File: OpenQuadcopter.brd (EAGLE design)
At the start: 100 x 100 mm, 36 parts, among them U1 MPU-6000QFN-24

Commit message: wrap up openquadcopter board.
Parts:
- moved JP1 1.92 mm to (-7.37, 18.2)
- moved U$12 1.30 mm to (-15.1, 12.6)
- moved C12 1.20 mm to (8.51, -8.89)
- moved U$9 1.02 mm to (32.0, -3.81)
- moved D4 1.02 mm to (21.2, -3.81)
- moved R4 1.02 mm to (15.5, 1.27)
- moved C1 1.02 mm to (-8.19, 7.76)
- moved U$3 1.02 mm to (3.43, 33.7)
- moved C11 1.02 mm to (11.7, -10.2)
- moved C2 1.02 mm to (-1.90, 13.1)
- moved C3 1.02 mm to (-5.46, 0.64)
- moved C4 1.02 mm to (4.06, 0.00)
- moved C5 1.02 mm to (-13.9, 2.69)
- moved C6 1.02 mm to (-12.1, 0.90)
- moved C7 1.02 mm to (-10.3, -0.90)
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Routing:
- net BAT: track 0.00 -> 148.6 mm, vias 0 -> 4
- net GND: track 0.00 -> 106.6 mm, vias 0 -> 8
- net VCC: track 0.00 -> 71.6 mm, vias 0 -> 5
- net MOTOR/PA6: track 0.00 -> 34.9 mm, vias 0 -> 2
- net N$10: track 0.00 -> 21.8 mm
- net INT/PA4: track 0.00 -> 20.8 mm, vias 0 -> 2
- net MOTOR/PA10: track 0.00 -> 17.4 mm
- net MOTOR/PA9: track 0.00 -> 17.2 mm
- net INT/PC0: track 0.00 -> 15.8 mm
- net MOTOR/PA7: track 0.00 -> 14.8 mm
- net N$7: track 0.00 -> 12.2 mm
- net N$5: track 0.00 -> 11.7 mm
- net SDL/PB6: track 0.00 -> 10.9 mm
- net N$1: track 0.00 -> 10.4 mm
- net N$2: track 0.00 -> 10.4 mm
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- added copper zone on layer 1, net GND
- added copper zone on layer 16, net GND

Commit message: Change the PWM's TIM. (Do not use TIM1 for pwm, since the pins are also related to SPI pins)
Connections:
- removed net MOTOR/PA6: R3.2, U$11.17, U$6.1
- removed net MOTOR/PA7: R4.2, U$11.19, U$8.1
- removed net PC8: U$11.4
- removed net PC9: U$11.9
- new net MOTOR/PC8: R4.2, U$11.4, U$8.1
- new net MOTOR/PC9: R3.2, U$11.9, U$6.1
- new net PA6: U$11.17
- new net PA7: U$11.19
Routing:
- net MOTOR/PA6: track 34.9 -> 0.00 mm, vias 2 -> 0
- net MOTOR/PC8: track 0.00 -> 33.2 mm, vias 0 -> 2
- net MOTOR/PC9: track 0.00 -> 26.6 mm
- net MOTOR/PA7: track 14.8 -> 0.00 mm
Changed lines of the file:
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@@
 <wire x1="-17.526" y1="-0.015" x2="-20.066" y2="-2.555" width="0.254" layer="1"/>
 </signal>
-<signal name="PC8">
+<signal name="MOTOR/PC8">
 <contactref element="U$11" pad="4"/>
+<contactref element="U$8" pad="1"/>
+<contactref element="R4" pad="2"/>
+<wire x1="-10.516" y1="6.38" x2="-10.516" y2="5.436" width="0.254" layer="1"/>
+<wire x1="-10.516" y1="5.436" x2="-9.906" y2="4.826" width="0.254" layer="1"/>
+<via x="-9.906" y="4.826" extent="1-16" drill="0.254"/>
+<wire x1="-9.906" y1="4.826" x2="-1.27" y2="4.826" width="0.254" layer="16"/>
+<wire x1="-1.27" y1="4.826" x2="-0.508" y2="4.064" width="0.254" layer="16"/>
+<wire x1="-0.508" y1="4.064" x2="14.732" y2="4.064" width="0.254" layer="16"/>
+<wire x1="14.732" y1="4.064" x2="15.494" y2="3.302" width="0.254" layer="16"/>
+<via x="15.494" y="3.302" extent="1-16" drill="0.254"/>
+<wire x1="15.494" y1="3.302" x2="15.494" y2="1.92" width="0.254" layer="1"/>
+<wire x1="19.274" y1="2.37" x2="15.944" y2="2.37" width="0.254" layer="1"/>
+<wire x1="15.944" y1="2.37" x2="15.494" y2="1.92" width="0.254" layer="1"/>
 </signal>
 <signal name="RESET">
@@
 <wire x1="-8.961" y1="-2.921" x2="-10.516" y2="-1.62" width="0.254" layer="1"/>
 </signal>
-<signal name="PC9">
+<signal name="MOTOR/PC9">
 <contactref element="U$11" pad="9"/>
+<contactref element="U$6" pad="1"/>
+<contactref element="R3" pad="2"/>
+<wire x1="-13.516" y1="-3.62" x2="-13.516" y2="-5.534" width="0.4064" layer="1"/>
+<wire x1="-13.516" y1="-5.534" x2="-5.08" y2="-13.97" width="0.4064" layer="1"/>
+<wire x1="-5.08" y1="-13.97" x2="-0.254" y2="-13.97" width="0.4064" layer="1"/>
+<wire x1="-0.254" y1="-13.97" x2="1.524" y2="-15.748" width="0.4064" layer="1"/>
+<wire x1="1.524" y1="-15.748" x2="1.524" y2="-17.765" width="0.4064" layer="1"/>
+<wire x1="1.524" y1="-17.765" x2="1.539" y2="-17.78" width="0.4064" layer="1"/>
+<wire x1="1.989" y1="-20.925" x2="1.989" y2="-18.23" width="0.4064" layer="1"/>
+<wire x1="1.989" y1="-18.23" x2="1.539" y2="-17.78" width="0.4064" layer="1"/>
 </signal>
 <signal name="PC5">
 <contactref element="U$11" pad="20"/>
 </signal>
-<signal name="MOTOR/PA7">
-<contactref element="U$11" pad="19"/>
-<contactref element="U$8" pad="1"/>
-<contactref element="R4" pad="2"/>
-<wire x1="11.484" y1="10.38" x2="12.734" y2="10.38" width="0.254" layer="1"/>
-<wire x1="12.734" y1="10.38" x2="15.494" y2="7.62" width="0.254" layer="1"/>
-<wire x1="15.494" y1="7.62" x2="15.494" y2="1.92" width="0.254" layer="1"/>
-<wire x1="15.494" y1="1.92" x2="18.824" y2="1.92" width="0.254" layer="1"/>
-<wire x1="18.824" y1="1.92" x2="19.274" y2="2.37" width="0.254" layer="1"/>
-</signal>
 <signal name="PA5">
 <contactref element="U$11" pad="18"/>
-</signal>
-<signal name="MOTOR/PA6">
-<contactref element="U$11" pad="17"/>
-<contactref element="U$6" pad="1"/>
-<contactref element="R3" pad="2"/>
-<wire x1="1.989" y1="-20.925" x2="1.989" y2="-18.23" width="0.254" layer="1"/>
-<wire x1="1.989" y1="-18.23" x2="1.539" y2="-17.78" width="0.254" layer="1"/>
-<wire x1="11.484" y1="6.38" x2="11.654" y2="6.38" width="0.254" layer="1"/>
-<wire x1="11.654" y1="6.38" x2="11.684" y2="6.35" width="0.254" layer="1"/>
-<wire x1="11.684" y1="6.35" x2="6.604" y2="6.35" width="0.254" layer="1"/>
-<wire x1="6.604" y1="6.35" x2="5.334" y2="5.08" width="0.254" layer="1"/>
-<via x="5.334" y="5.08" extent="1-16" drill="0.254"/>
-<wire x1="5.334" y1="5.08" x2="5.334" y2="-8.89" width="0.254" layer="16"/>
-<wire x1="5.334" y1="-8.89" x2="1.524" y2="-12.7" width="0.254" layer="16"/>
-<via x="1.524" y="-12.7" extent="1-16" drill="0.254"/>
-<wire x1="1.524" y1="-12.7" x2="1.524" y2="-17.765" width="0.254" layer="1"/>
-<wire x1="1.524" y1="-17.765" x2="1.539" y2="-17.78" width="0.254" layer="1"/>
 </signal>
 <signal name="INT/PC0">
@@
 <wire x1="11.572" y1="-10.922" x2="11.684" y2="-10.81" width="0.254" layer="1"/>
 </signal>
+<signal name="PA7">
+<contactref element="U$11" pad="19"/>
+</signal>
+<signal name="PA6">
+<contactref element="U$11" pad="17"/>
+</signal>
 </signals>

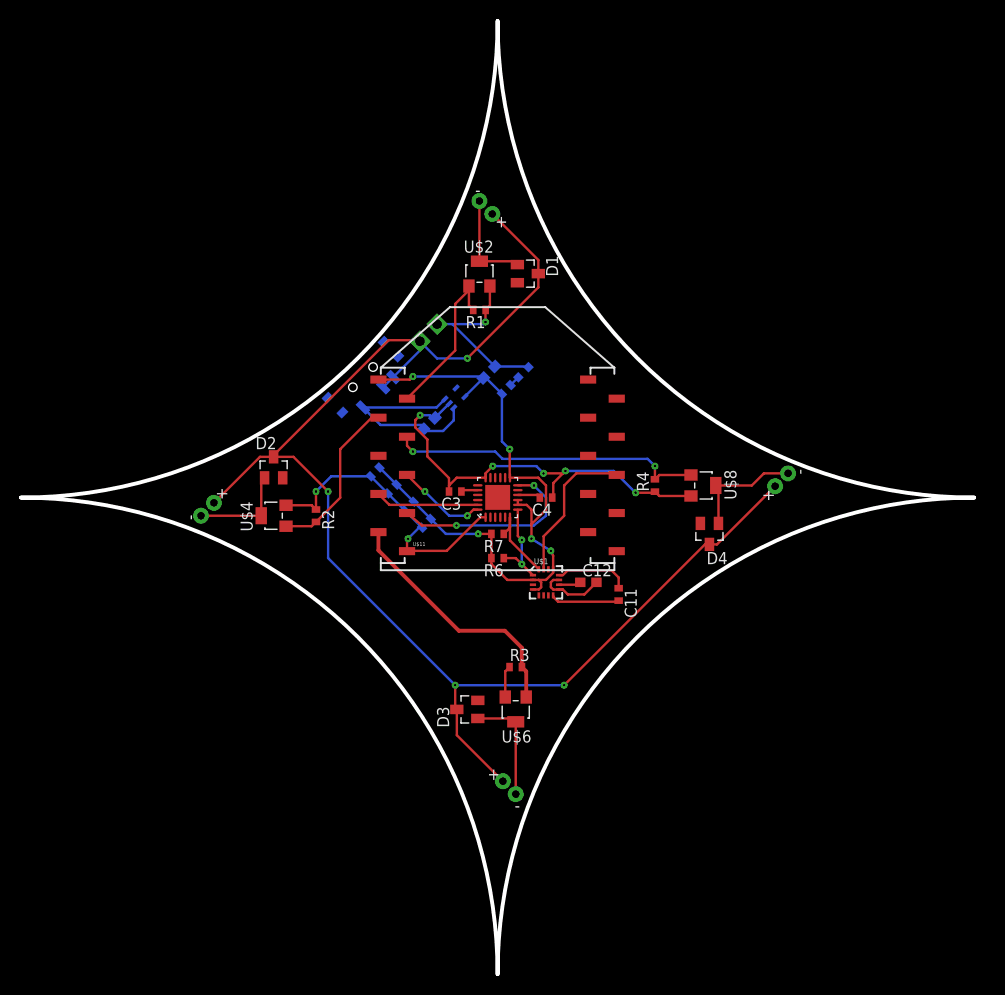
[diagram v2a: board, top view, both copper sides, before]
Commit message: Add holes as a pendant.
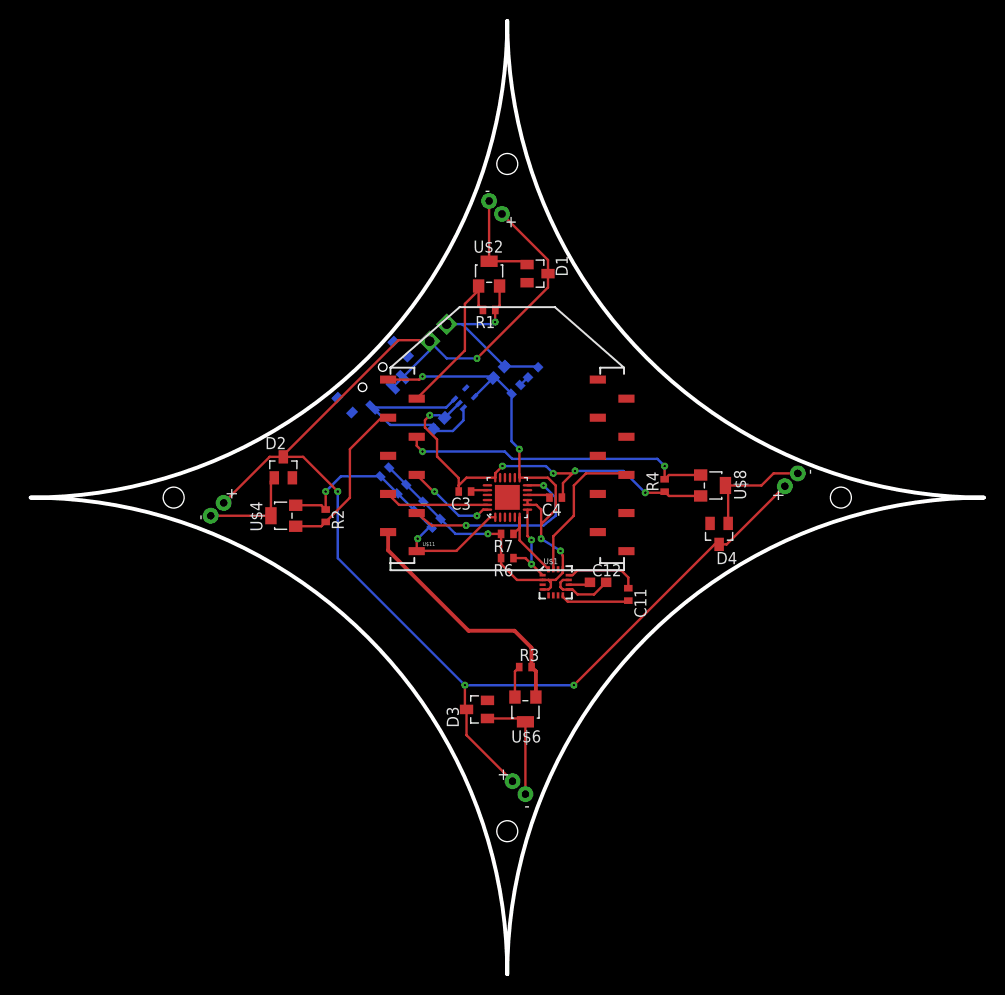
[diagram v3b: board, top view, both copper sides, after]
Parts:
- moved U$9 1.02 mm to (33.0, -3.81)
- moved D4 1.02 mm to (22.2, -3.81)
- moved R4 1.02 mm to (16.5, 1.27)
- moved C1 1.02 mm to (-7.17, 7.76)
- moved U$3 1.02 mm to (4.45, 33.7)
- moved C11 1.02 mm to (12.7, -10.2)
- moved C12 1.02 mm to (9.53, -8.89)
- moved C2 1.02 mm to (-0.88, 13.1)
- moved C3 1.02 mm to (-4.45, 0.64)
- moved C4 1.02 mm to (5.08, 0.00)
- moved C5 1.02 mm to (-12.9, 2.69)
- moved C6 1.02 mm to (-11.1, 0.90)
- moved C7 1.02 mm to (-9.26, -0.90)
- moved D1 1.02 mm to (3.17, 23.5)
- moved D3 1.02 mm to (-3.17, -22.2)
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
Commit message: update openquadcopter.
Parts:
- removed LED1: (no value), led:CHIP-LED0603
- added D5: GREEN, openmotestm:LED-0603
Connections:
- removed net MOTOR/PA10: R2.2, U$11.3, U$4.1
- removed net MOTOR/PA9: R1.2, U$11.2, U$2.1
- removed net N$15: LED1.A, R5.1
- removed net PA6: U$11.17
- removed net PA7: U$11.19
- new net MOTOR/PA6: R3.2, U$11.17, U$6.1
- new net MOTOR/PA7: R4.2, U$11.19, U$8.1
- new net N$17: D5.A, R5.1
- new net PA10: U$11.3
- new net PA9: U$11.2
- net GND: now also D5.C; no longer LED1.C
- net MOTOR/PC8: now also R1.2, U$2.1; no longer R4.2, U$8.1
- net MOTOR/PC9: now also R2.2, U$4.1; no longer R3.2, U$6.1
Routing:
- net MOTOR/PA6: track 0.00 -> 34.0 mm, vias 0 -> 2
- net MOTOR/PA10: track 17.4 -> 0.00 mm
- net MOTOR/PA9: track 17.2 -> 0.00 mm
- net MOTOR/PC9: track 26.6 -> 10.3 mm
- net MOTOR/PC8: track 33.2 -> 19.0 mm, vias 2 -> 0
- net MOTOR/PA7: track 0.00 -> 14.1 mm
- net GND: track 106.6 -> 101.9 mm
- net N$17: track 0.00 -> 1.84 mm
- net N$15: track 1.14 -> 0.00 mm
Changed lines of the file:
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@@
 <layer number="220" name="220bmp" color="21" fill="1" visible="no" active="no"/>
 <layer number="221" name="221bmp" color="22" fill="1" visible="no" active="no"/>
-<layer number="222" name="222bmp" color="23" fill="1" visible="no" active="no"/>
 <layer number="223" name="223bmp" color="24" fill="1" visible="no" active="no"/>
 <layer number="224" name="224bmp" color="25" fill="1" visible="no" active="no"/>
@@
 <element name="JP1" library="SparkFun-Connectors" package="1X02_2.54_SCREWTERM" value="2.54MM" x="-6.35" y="18.1971" rot="MR315"/>
 <element name="C1" library="rcl" package="C0603" value="" x="-7.1709875" y="7.76085625" rot="MR135"/>
-<element name="LED1" library="led" package="CHIP-LED0603" value="" x="2.70729375" y="13.1490125" rot="MR45"/>
 <element name="C3" library="rcl" package="C0402" value="100nF" x="-4.445" y="0.635" rot="R180"/>
 <element name="C4" library="rcl" package="C0402" value="2.2nF" x="5.08" y="0" rot="R180"/>
@@
 <element name="R5" library="rcl" package="R0402" value="" x="0.911240625" y="11.352959375" rot="MR315"/>
 <element name="C2" library="rcl" package="C0603" value="" x="-0.884809375" y="13.1490125" rot="MR315"/>
+<element name="D5" library="openmotestm" package="LED-0603" value="GREEN" x="3.302" y="9.906" rot="MR135">
+<attribute name="PROD_ID" value="DIO-00821" x="3.302" y="9.906" size="1.778" layer="28" rot="MR135" display="off"/>
+</element>
 </elements>
 <signals>
@@
 <contactref element="U$10" pad="2"/>
 <contactref element="C1" pad="2"/>
-<contactref element="LED1" pad="C"/>
 <contactref element="U$11" pad="10"/>
 <contactref element="U1" pad="18"/>
@@
 <contactref element="C7" pad="2"/>
 <contactref element="C9" pad="2"/>
-<contactref element="C2" pad="1"/>
-<wire x1="-6.35" y1="18.1971" x2="-4.730815625" y2="18.1971" width="0.254" layer="16"/>
-<wire x1="-4.730815625" y1="18.1971" x2="-0.28376875" y2="13.750053125" width="0.254" layer="16"/>
-<wire x1="-0.28376875" y1="13.750053125" x2="3.1669125" y2="13.750053125" width="0.254" layer="16"/>
-<wire x1="3.1669125" y1="13.750053125" x2="3.237625" y2="13.679340625" width="0.254" layer="16"/>
 <wire x1="-6.569946875" y1="8.361896875" x2="-5.060278125" y2="9.87156875" width="0.254" layer="16"/>
 <wire x1="20.29" y1="0.17" x2="16.96" y2="0.17" width="0.254" layer="1"/>
@@
 <wire x1="-0.805" y1="22.195" x2="-0.805" y2="20.135" width="0.254" layer="1"/>
 <wire x1="-0.805" y1="20.135" x2="-1.255" y2="19.685" width="0.254" layer="1"/>
-<wire x1="-4.730815625" y1="18.1971" x2="-1.4879" y2="18.1971" width="0.254" layer="16"/>
+<wire x1="-6.35" y1="18.1971" x2="-1.4879" y2="18.1971" width="0.254" layer="16"/>
 <wire x1="-1.4879" y1="18.1971" x2="-1.27" y2="18.415" width="0.254" layer="16"/>
 <via x="-1.27" y="18.415" extent="1-16" drill="0.254"/>
@@
 <contactref element="R3" pad="1"/>
 <wire x1="0.805" y1="-18.23" x2="1.255" y2="-17.78" width="0.254" layer="1"/>
+<contactref element="C2" pad="1"/>
+<contactref element="D5" pad="C"/>
+<wire x1="-0.28376875" y1="13.750053125" x2="-0.28376875" y2="17.42876875" width="0.254" layer="16"/>
+<wire x1="-0.28376875" y1="17.42876875" x2="-1.27" y2="18.415" width="0.254" layer="16"/>
 </signal>
 <signal name="N$1">
@@
 <wire x1="1.2967" y1="2.0862" x2="1.27" y2="2.1129" width="0" layer="19" extent="1-1"/>
 </signal>
-<signal name="MOTOR/PA9">
-<contactref element="U$11" pad="2"/>
+<signal name="MOTOR/PC8">
 <contactref element="U$2" pad="1"/>
 <contactref element="R1" pad="2"/>
-<wire x1="-3.005" y1="22.195" x2="-3.005" y2="21.76" width="0.254" layer="1"/>
-<wire x1="-3.005" y1="21.76" x2="-4.445" y2="20.32" width="0.254" layer="1"/>
-<wire x1="-4.445" y1="20.32" x2="-4.445" y2="15.435" width="0.254" layer="1"/>
-<wire x1="-4.445" y1="15.435" x2="-9.5" y2="10.38" width="0.254" layer="1"/>
-<wire x1="-3.005" y1="22.195" x2="-3.005" y2="20.135" width="0.254" layer="1"/>
-<wire x1="-3.005" y1="20.135" x2="-2.555" y2="19.685" width="0.254" layer="1"/>
-</signal>
-<signal name="MOTOR/PA10">
-<contactref element="U$11" pad="3"/>
-<contactref element="U$4" pad="1"/>
-<contactref element="R2" pad="2"/>
-<wire x1="-22.195" y1="-3.005" x2="-19.5" y2="-3.005" width="0.254" layer="1"/>
-<wire x1="-19.5" y1="-3.005" x2="-19.05" y2="-2.555" width="0.254" layer="1"/>
-<wire x1="-12.5" y1="8.38" x2="-13.21" y2="8.38" width="0.254" layer="1"/>
-<wire x1="-13.21" y1="8.38" x2="-16.51" y2="5.08" width="0.254" layer="1"/>
-<wire x1="-16.51" y1="5.08" x2="-16.51" y2="-0.015" width="0.254" layer="1"/>
-<wire x1="-16.51" y1="-0.015" x2="-19.05" y2="-2.555" width="0.254" layer="1"/>
-</signal>
-<signal name="MOTOR/PC8">
 <contactref element="U$11" pad="4"/>
-<contactref element="U$8" pad="1"/>
-<contactref element="R4" pad="2"/>
-<wire x1="-9.5" y1="6.38" x2="-9.5" y2="5.436" width="0.254" layer="1"/>
-<wire x1="-9.5" y1="5.436" x2="-8.89" y2="4.826" width="0.254" layer="1"/>
-<via x="-8.89" y="4.826" extent="1-16" drill="0.254"/>
-<wire x1="-8.89" y1="4.826" x2="-0.254" y2="4.826" width="0.254" layer="16"/>
-<wire x1="-0.254" y1="4.826" x2="0.508" y2="4.064" width="0.254" layer="16"/>
-<wire x1="0.508" y1="4.064" x2="15.748" y2="4.064" width="0.254" layer="16"/>
-<wire x1="15.748" y1="4.064" x2="16.51" y2="3.302" width="0.254" layer="16"/>
-<via x="16.51" y="3.302" extent="1-16" drill="0.254"/>
-<wire x1="16.51" y1="3.302" x2="16.51" y2="1.92" width="0.254" layer="1"/>
-<wire x1="20.29" y1="2.37" x2="16.96" y2="2.37" width="0.254" layer="1"/>
-<wire x1="16.96" y1="2.37" x2="16.51" y2="1.92" width="0.254" layer="1"/>
+<wire x1="-2.555" y1="19.685" x2="-2.555" y2="21.745" width="0.254" layer="1"/>
+<wire x1="-2.555" y1="21.745" x2="-3.005" y2="22.195" width="0.254" layer="1"/>
+<wire x1="-2.555" y1="19.685" x2="-2.555" y2="17.765" width="0.254" layer="1"/>
+<wire x1="-2.555" y1="17.765" x2="-6.35" y2="13.97" width="0.254" layer="1"/>
+<wire x1="-6.35" y1="13.97" x2="-6.35" y2="11.684" width="0.254" layer="1"/>
+<wire x1="-6.35" y1="11.684" x2="-9.652" y2="8.382" width="0.254" layer="1"/>
+<wire x1="-9.652" y1="8.382" x2="-9.652" y2="6.532" width="0.254" layer="1"/>
+<wire x1="-9.652" y1="6.532" x2="-9.5" y2="6.38" width="0.254" layer="1"/>
 </signal>
 <signal name="RESET">
@@
 </signal>
 <signal name="MOTOR/PC9">
+<contactref element="U$4" pad="1"/>
+<contactref element="R2" pad="2"/>
 <contactref element="U$11" pad="9"/>
-<contactref element="U$6" pad="1"/>
-<contactref element="R3" pad="2"/>
-<wire x1="-12.5" y1="-3.62" x2="-12.5" y2="-5.534" width="0.4064" layer="1"/>
-<wire x1="-12.5" y1="-5.534" x2="-4.064" y2="-13.97" width="0.4064" layer="1"/>
-<wire x1="-4.064" y1="-13.97" x2="0.762" y2="-13.97" width="0.4064" layer="1"/>
-<wire x1="0.762" y1="-13.97" x2="2.54" y2="-15.748" width="0.4064" layer="1"/>
-<wire x1="2.54" y1="-15.748" x2="2.54" y2="-17.765" width="0.4064" layer="1"/>
-<wire x1="2.54" y1="-17.765" x2="2.555" y2="-17.78" width="0.4064" layer="1"/>
-<wire x1="3.005" y1="-20.925" x2="3.005" y2="-18.23" width="0.4064" layer="1"/>
-<wire x1="3.005" y1="-18.23" x2="2.555" y2="-17.78" width="0.4064" layer="1"/>
+<wire x1="-19.05" y1="-2.555" x2="-21.745" y2="-2.555" width="0.254" layer="1"/>
+<wire x1="-21.745" y1="-2.555" x2="-22.195" y2="-3.005" width="0.254" layer="1"/>
+<wire x1="-19.05" y1="-2.555" x2="-13.565" y2="-2.555" width="0.254" layer="1"/>
+<wire x1="-13.565" y1="-2.555" x2="-12.5" y2="-3.62" width="0.254" layer="1"/>
 </signal>
 <signal name="PC5">
@@
 <wire x1="8.29" y1="-9.14" x2="8.675" y2="-8.89" width="0.254" layer="1"/>
 </signal>
-<signal name="N$15">
-<contactref element="LED1" pad="A"/>
-<contactref element="R5" pad="1"/>
-<wire x1="1.3708625" y1="11.812578125" x2="2.176965625" y2="12.61868125" width="0.254" layer="16"/>
-</signal>
 <signal name="N$13">
 <contactref element="C11" pad="1"/>
@@
 <wire x1="12.588" y1="-10.922" x2="12.7" y2="-10.81" width="0.254" layer="1"/>
 </signal>
-<signal name="PA7">
+<signal name="MOTOR/PA7">
+<contactref element="U$8" pad="1"/>
+<contactref element="R4" pad="2"/>
 <contactref element="U$11" pad="19"/>
-</signal>
-<signal name="PA6">
+<wire x1="20.29" y1="2.37" x2="16.96" y2="2.37" width="0.254" layer="1"/>
+<wire x1="16.96" y1="2.37" x2="16.51" y2="1.92" width="0.254" layer="1"/>
+<wire x1="16.51" y1="1.92" x2="16.51" y2="6.37" width="0.254" layer="1"/>
+<wire x1="16.51" y1="6.37" x2="12.5" y2="10.38" width="0.254" layer="1"/>
+</signal>
+<signal name="MOTOR/PA6">
+<contactref element="U$6" pad="1"/>
+<contactref element="R3" pad="2"/>
 <contactref element="U$11" pad="17"/>
+<wire x1="3.005" y1="-20.925" x2="3.005" y2="-18.23" width="0.254" layer="1"/>
+<wire x1="3.005" y1="-18.23" x2="2.555" y2="-17.78" width="0.254" layer="1"/>
+<wire x1="12.5" y1="6.38" x2="12.67" y2="6.38" width="0.254" layer="1"/>
+<wire x1="12.67" y1="6.38" x2="15.24" y2="3.81" width="0.254" layer="1"/>
+<via x="15.24" y="3.81" extent="1-16" drill="0.6" shape="square"/>
+<wire x1="15.24" y1="3.81" x2="15.24" y2="-1.27" width="0.254" layer="16"/>
+<wire x1="15.24" y1="-1.27" x2="2.54" y2="-13.97" width="0.254" layer="16"/>
+<via x="2.54" y="-13.97" extent="1-16" drill="0.254"/>
+<wire x1="2.54" y1="-13.97" x2="2.54" y2="-17.765" width="0.254" layer="1"/>
+<wire x1="2.54" y1="-17.765" x2="2.555" y2="-17.78" width="0.254" layer="1"/>
+</signal>
+<signal name="N$17">
+<contactref element="R5" pad="1"/>
+<contactref element="D5" pad="A"/>
+<wire x1="1.3708625" y1="11.812578125" x2="1.395421875" y2="11.812578125" width="0.254" layer="16"/>
+<wire x1="1.395421875" y1="11.812578125" x2="2.68186875" y2="10.52613125" width="0.254" layer="16"/>
+</signal>
+<signal name="PA9">
+<contactref element="U$11" pad="2"/>
+</signal>
+<signal name="PA10">
+<contactref element="U$11" pad="3"/>
 </signal>
 </signals>
